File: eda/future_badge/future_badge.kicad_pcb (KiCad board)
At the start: 2 copper layers, 0 parts

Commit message: updated schematic
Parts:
- added C11: 100nF, 0_local:C_Disc_D3.0mm_W2.0mm_P2.50mm_backsilk, F.Cu at (135.8, 124.7)
- added C12: 100nF, 0_local:C_Disc_D3.0mm_W2.0mm_P2.50mm_backsilk, F.Cu at (139.0, 93.3)
- added C21: 100nF, 0_local:C_Disc_D3.0mm_W2.0mm_P2.50mm_backsilk, F.Cu at (148.0, 89.6)
- added C22: 100nF, 0_local:C_Disc_D3.0mm_W2.0mm_P2.50mm_backsilk, F.Cu at (139.8, 83.2)
- added D1: LED_Two_Color_CC_THT_3mm, 0_local:LED_D3.0mm-3-TwoColor, F.Cu at (169.4, 75.4)
- added D11: LED_WS2812D_THT_5mm, 0_local:LED_D5.0mm-4_WS2812D_front_new, F.Cu at (151.6, 73.0)
- added D12: LED_WS2812D_THT_5mm, 0_local:LED_D5.0mm-4_WS2812D_front_new, F.Cu at (137.4, 70.6)
- added D21: LED_WS2812D_THT_5mm, 0_local:LED_D5.0mm-4_WS2812D_front_new, F.Cu at (114.6, 67.0)
- added D22: LED_WS2812D_THT_5mm, 0_local:LED_D5.0mm-4_WS2812D_front_new, F.Cu at (127.2, 69.6)
- added U1: ESP32-WROOM-32-DEVKIT, 0_local:ESP32_DEVKIT_V1, F.Cu at (104.5, 103.7)

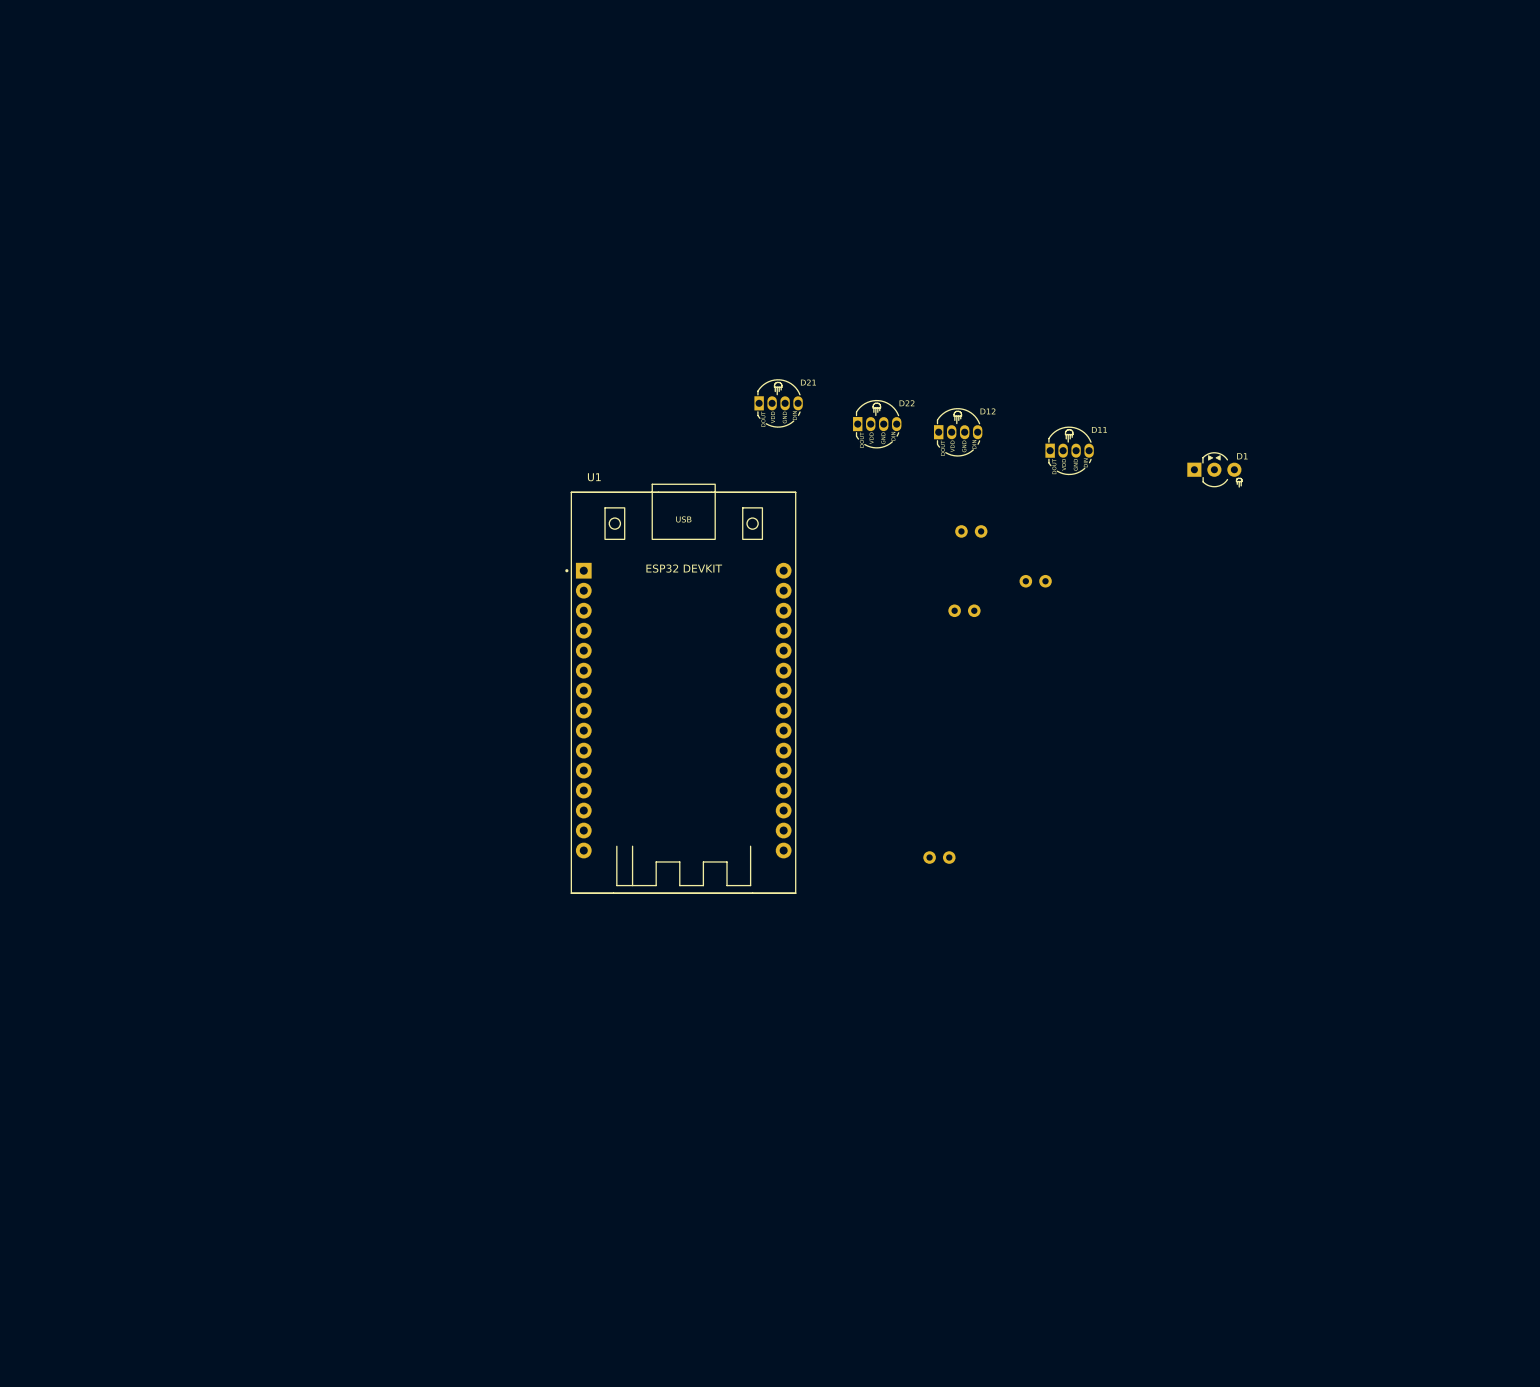
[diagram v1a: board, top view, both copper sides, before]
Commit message: schematic and code and art updates
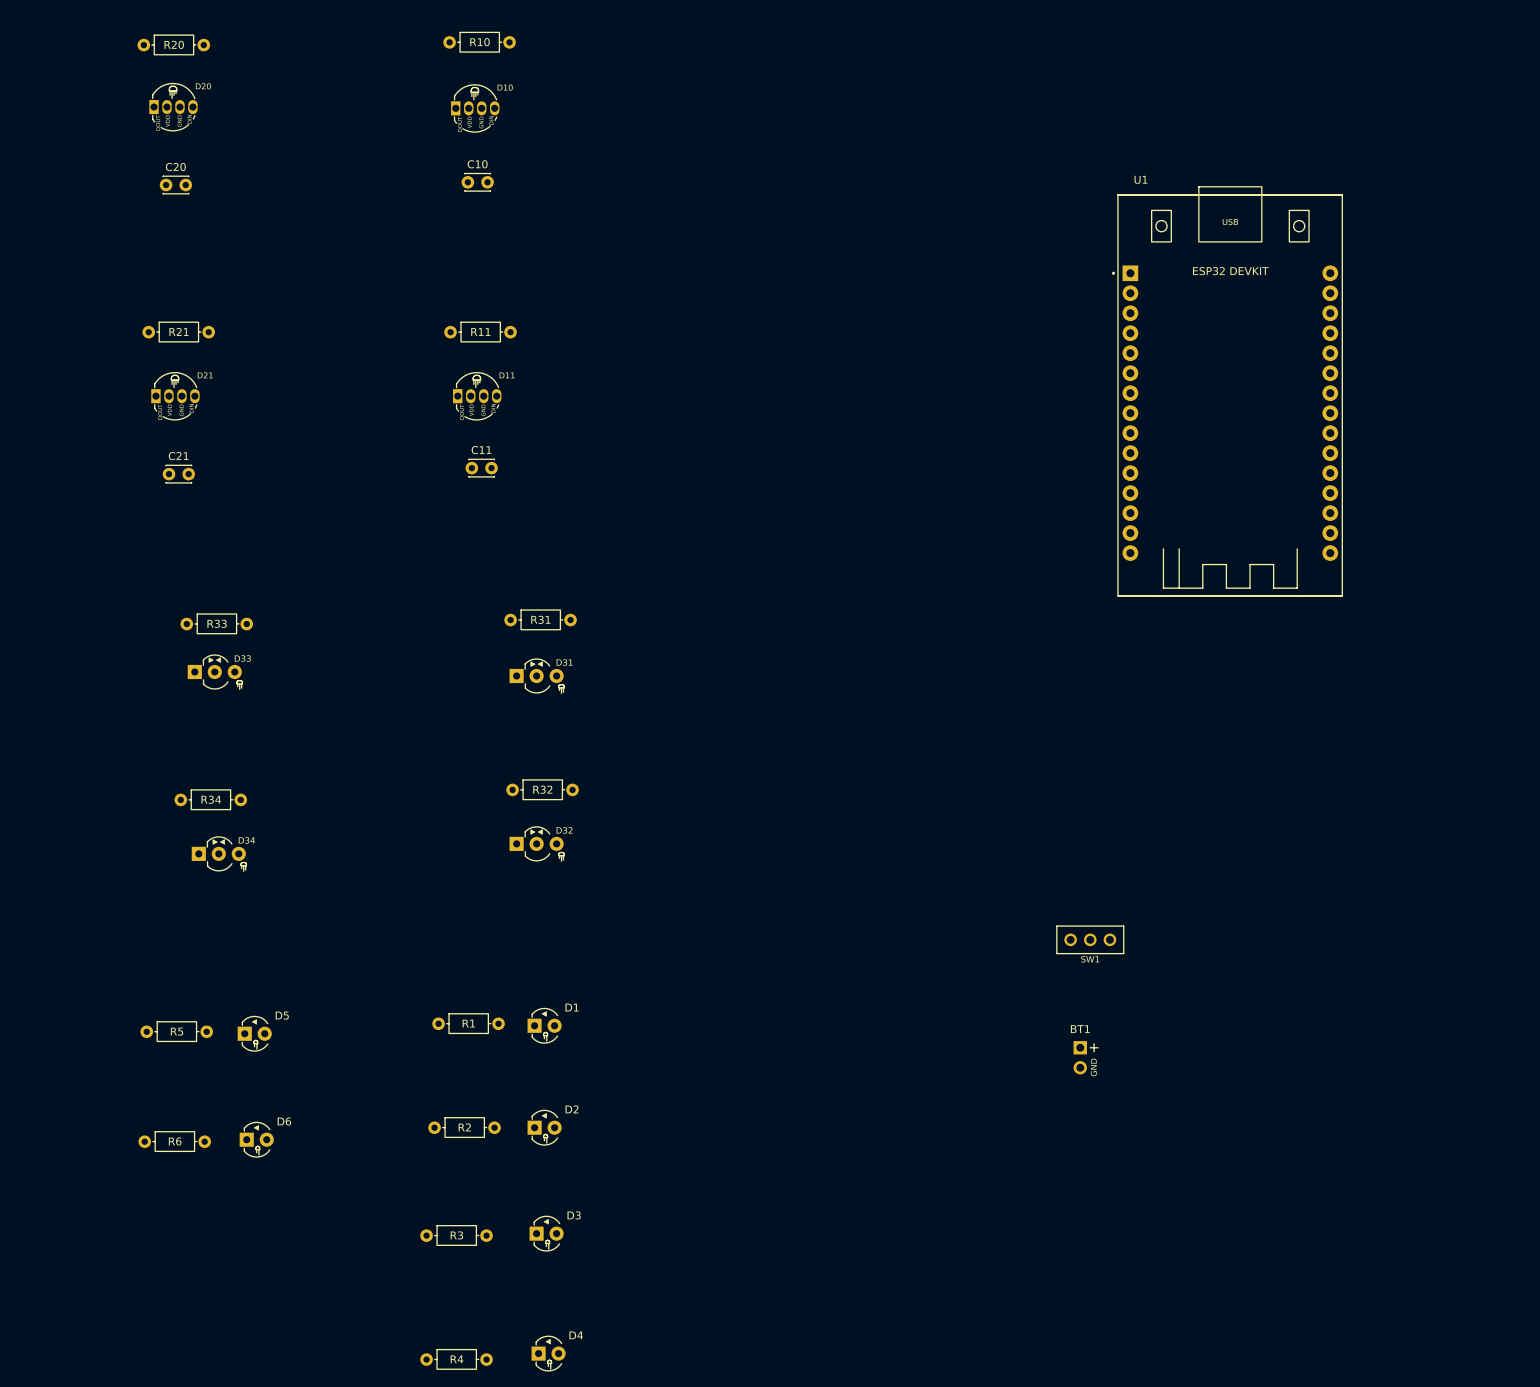
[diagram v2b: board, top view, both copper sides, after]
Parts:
- removed C12, C22: 100nF, 0_local:C_Disc_D3.0mm_W2.0mm_P2.50mm_backsilk
- removed D12, D22: LED_WS2812D_THT_5mm, 0_local:LED_D5.0mm-4_WS2812D_front_new
- added BT1: Battery_9V, 0_local:Battery_Lead_Wire_Connector, F.Cu at (154.9, 148.8)
- added C10: 100nF, 0_local:C_Disc_D3.0mm_W2.0mm_P2.50mm, F.Cu at (77.1, 38.9)
- added C20: 100nF, 0_local:C_Disc_D3.0mm_W2.0mm_P2.50mm, F.Cu at (38.8, 39.2)
- added D10: LED_WS2812D_5mm, 0_local:LED_D5.0mm-4_WS2812D_front_new, F.Cu at (76.1, 29.5)
- added D2: LED_3mm, 0_local:LED_D3.0mm-2, F.Cu at (85.6, 159.0)
- added D20: LED_WS2812D_5mm, 0_local:LED_D5.0mm-4_WS2812D_front_new, F.Cu at (37.7, 29.3)
- added D3: LED_3mm, 0_local:LED_D3.0mm-2, F.Cu at (85.8, 172.5)
- added D31: YEL_RED_CC_3mm, 0_local:LED_D3.0mm-3-TwoColor, F.Cu at (83.3, 101.6)
- added D32: YEL_RED_CC_3mm, 0_local:LED_D3.0mm-3-TwoColor, F.Cu at (83.3, 122.9)
- added D33: YEL_RED_CC_3mm, 0_local:LED_D3.0mm-3-TwoColor, F.Cu at (42.4, 101.1)
- added D34: YEL_RED_CC_3mm, 0_local:LED_D3.0mm-3-TwoColor, F.Cu at (42.9, 124.2)
- added D4: LED_3mm, 0_local:LED_D3.0mm-2, F.Cu at (86.1, 187.7)
- added D5: LED_3mm, 0_local:LED_D3.0mm-2, F.Cu at (48.8, 147.1)
- added D6: LED_3mm, 0_local:LED_D3.0mm-2, F.Cu at (49.0, 160.5)
- added R1: 47R_6.3mm, 0_local:R_Axial_DIN0207_L6.3mm_D2.5mm_P7.62mm_Horizontal, F.Cu at (73.4, 145.8)
- added R10: 47R_6.3mm, 0_local:R_Axial_DIN0207_L6.3mm_D2.5mm_P7.62mm_Horizontal, F.Cu at (74.8, 21.1)
- added R11: 47R_6.3mm, 0_local:R_Axial_DIN0207_L6.3mm_D2.5mm_P7.62mm_Horizontal, F.Cu at (74.9, 57.9)
- added R2: 47R_6.3mm, 0_local:R_Axial_DIN0207_L6.3mm_D2.5mm_P7.62mm_Horizontal, F.Cu at (72.9, 159.0)
- added R20: 47R_6.3mm, 0_local:R_Axial_DIN0207_L6.3mm_D2.5mm_P7.62mm_Horizontal, F.Cu at (35.9, 21.4)
- added R21: 47R_6.3mm, 0_local:R_Axial_DIN0207_L6.3mm_D2.5mm_P7.62mm_Horizontal, F.Cu at (36.6, 57.9)
- added R3: 47R_6.3mm, 0_local:R_Axial_DIN0207_L6.3mm_D2.5mm_P7.62mm_Horizontal, F.Cu at (71.9, 172.7)
- added R31: 47R_6.3mm, 0_local:R_Axial_DIN0207_L6.3mm_D2.5mm_P7.62mm_Horizontal, F.Cu at (82.5, 94.5)
- added R32: 47R_6.3mm, 0_local:R_Axial_DIN0207_L6.3mm_D2.5mm_P7.62mm_Horizontal, F.Cu at (82.8, 116.1)
- added R33: 47R_6.3mm, 0_local:R_Axial_DIN0207_L6.3mm_D2.5mm_P7.62mm_Horizontal, F.Cu at (41.4, 95.0)
- added R34: 47R_6.3mm, 0_local:R_Axial_DIN0207_L6.3mm_D2.5mm_P7.62mm_Horizontal, F.Cu at (40.6, 117.3)
- added R4: 47R_6.3mm, 0_local:R_Axial_DIN0207_L6.3mm_D2.5mm_P7.62mm_Horizontal, F.Cu at (71.9, 188.5)
- added R5: 47R_6.3mm, 0_local:R_Axial_DIN0207_L6.3mm_D2.5mm_P7.62mm_Horizontal, F.Cu at (36.3, 146.8)
- added R6: 47R_6.3mm, 0_local:R_Axial_DIN0207_L6.3mm_D2.5mm_P7.62mm_Horizontal, F.Cu at (36.1, 160.8)
- added SW1: SPDT_SS12D00G, 0_local:SW_SPDT_Slide_SS12D00G-1P2T_3pin, F.Cu at (156.2, 135.1)
- C11, C21: footprint 0_local:C_Disc_D3.0mm_W2.0mm_P2.50mm_backsilk -> 0_local:C_Disc_D3.0mm_W2.0mm_P2.50mm
- D1: value LED_Two_Color_CC_THT_3mm -> LED_3mm; footprint 0_local:LED_D3.0mm-3-TwoColor -> 0_local:LED_D3.0mm-2
- D11, D21: value LED_WS2812D_THT_5mm -> LED_WS2812D_5mm
- moved C21 109.7 mm to (39.1, 75.9)
- moved D1 109.7 mm to (85.6, 146.1)
- moved U1 79.1 mm to (174.0, 65.9)
- moved D21 76.7 mm to (38.0, 66.0)
- moved C11 76.4 mm to (77.6, 75.2)
- moved D11 75.6 mm to (76.3, 66.0)
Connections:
- D1 pad 1: LED31 -> Net-(D1-Pad1)
- D1 pad 2: GND -> LED01
- D11 pad 1: NEO1-1 -> unconnected-(D11-Pad1)
- D11 pad 4: NEO1 -> Net-(D11-Pad4)
- D21 pad 1: NEO2-1 -> unconnected-(D21-Pad1)
- D21 pad 4: NEO2 -> Net-(D21-Pad4)
- U1 pad 11: unconnected-(U1-Pad11) -> LED03
- U1 pad 14: unconnected-(U1-Pad14) -> LED02
- U1 pad 15: unconnected-(U1-Pad15) -> LED01
- U1 pad 21: TCH1 -> LED34A
- U1 pad 22: unconnected-(U1-Pad22) -> LED34B
- U1 pad 23: unconnected-(U1-Pad23) -> LED33A
- U1 pad 24: unconnected-(U1-Pad24) -> LED33B
- U1 pad 25: unconnected-(U1-Pad25) -> LED32A
- U1 pad 26: unconnected-(U1-Pad26) -> LED32B
- U1 pad 27: LED31 -> LED31A
- U1 pad 28: LED32 -> LED31B
- U1 pad 29: unconnected-(U1-Pad29) -> GND
- U1 pad 30: unconnected-(U1-Pad30) -> +9V
- U1 pad 5: unconnected-(U1-Pad5) -> TOUCH
- U1 pad 6: unconnected-(U1-Pad6) -> LED06
- U1 pad 7: unconnected-(U1-Pad7) -> LED05
- U1 pad 8: unconnected-(U1-Pad8) -> LED04

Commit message: art and footprint and pcb updates
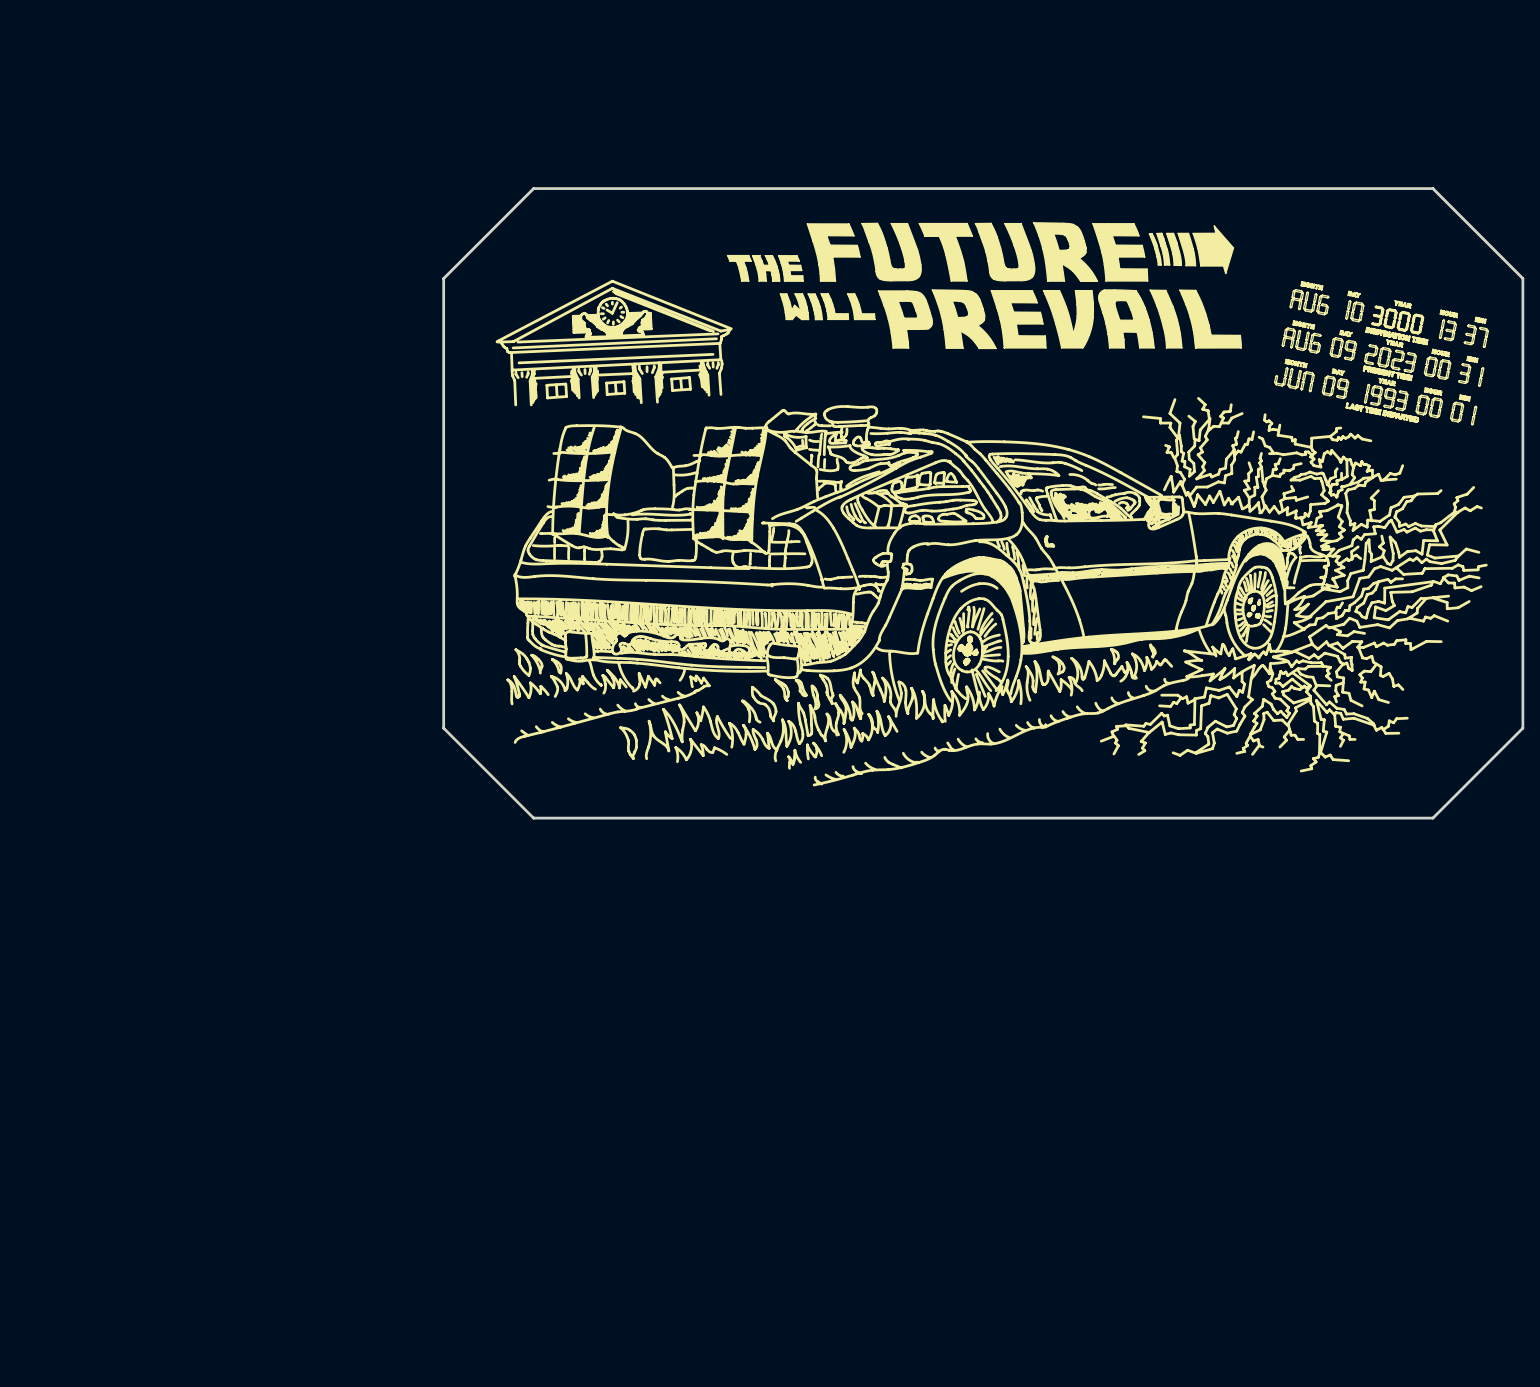
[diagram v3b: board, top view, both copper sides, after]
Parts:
- removed BT1: Battery_9V, 0_local:Battery_Lead_Wire_Connector
- removed C10, C11, C20, C21: 100nF, 0_local:C_Disc_D3.0mm_W2.0mm_P2.50mm
- removed D1, D2, D3, D4, D5, D6: LED_3mm, 0_local:LED_D3.0mm-2
- removed D10, D11, D20, D21: LED_WS2812D_5mm, 0_local:LED_D5.0mm-4_WS2812D_front_new
- removed D31, D32, D33, D34: YEL_RED_CC_3mm, 0_local:LED_D3.0mm-3-TwoColor
- removed R1, R10, R11, R2, R20, R21, R3, R31, R32, R33, R34, R4, R5, R6: 47R_6.3mm, 0_local:R_Axial_DIN0207_L6.3mm_D2.5mm_P7.62mm_Horizontal
- removed SW1: SPDT_SS12D00G, 0_local:SW_SPDT_Slide_SS12D00G-1P2T_3pin
- removed U1: ESP32-WROOM-32-DEVKIT, 0_local:ESP32_DEVKIT_V1
- added REF**: future_badge_frontmask_flames, 0_local:future_badge_frontmask_flames, F.Cu at (140.2, 77.2)
- added REF**: future_badge_frontsilk_title_txt, 0_local:future_badge_frontsilk_title_txt, F.Cu at (147.1, 63.8)
- added REF**: future_badge_edgecuts, 0_local:future_badge_edgecuts, F.Cu at (141.0, 73.7)
- added REF**: future_badge_frontmask_lightning, 0_local:future_badge_frontmask_lightning, F.Cu at (145.3, 71.4)
- added REF**: future_badge_frontsilk_notxt, 0_local:future_badge_frontsilk_notxt, F.Cu at (145.3, 58.9)
- added REF**: future_badge_frontsilk_panel, 0_local:future_badge_frontsilk_panel, F.Cu at (141.7, 72.6)
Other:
- board outline added: 137.1 x 80 mm
